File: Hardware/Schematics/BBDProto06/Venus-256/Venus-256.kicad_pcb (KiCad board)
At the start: 2 copper layers, 172.7 x 109.2 mm, 189 parts, among them J1 RaspberryPi header, J10 S08, J11 S09, J12 S10, J13 S11, J14 S12, J15 S13, J16 S14, J17 S15, J18 S16, J2 ARM JTAG, J23 S01, J24 S02, J25 S03, J26 S04, J27 S05, J28 S06, J29 S07, J3 S01, J30 S08, J31 S09, J32 S10, J33 S11, J34 S12, J35 S13, J36 S14, J37 S15, J38 S16, J4 S02, J40 S01, J41 S02, J42 S03, J43 S04, J44 S05, J45 S06, J46 S07, J47 S08, J48 S09, J49 S10, J5 S03, J50 S11, J51 S12, J52 S13, J53 S14, J54 S15, J55 S16, J57 S01, J58 S02, J59 S03, J6 S04, J60 S04, J61 S05, J62 S06, J63 S07, J64 S08, J65 S09, J66 S10, J67 S11, J68 S12, J69 S13, J7 S05, J70 S14, J71 S15, J72 S16, J8 S06, J9 S07, U1 ADG715, U2 AD7616, U3 ATSAME70Q21A-AN, U4 AD7616, U5 AD7616, U6 AD7616, U7 ATSAME70Q21A-AN

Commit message: Added a 5th cell-slave
Added a 5th cell-slave
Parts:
- removed C1, C13, C16, C3, C38, C39, C41, C45, C48, C6, C7, C9: 10uF, Capacitor_SMD:C_0603_1608Metric_Pad0.84x1.00mm_HandSolder
- removed C10, C12, C15, C2, C37, C4, C40, C42, C44, C47, C5, C8: 0.1uF, Capacitor_SMD:C_0603_1608Metric_Pad0.84x1.00mm_HandSolder
- removed C11, C43: 10uF,X5R, Capacitor_SMD:C_0603_1608Metric_Pad0.84x1.00mm_HandSolder
- removed C14, C46: 0.1uF,X8R, Capacitor_SMD:C_0603_1608Metric_Pad0.84x1.00mm_HandSolder
- removed J10, J30, J47, J64: S08, Connector_Wire:SolderWirePad_single_0-8mmDrill
- removed J11, J31, J48, J65: S09, Connector_Wire:SolderWirePad_single_0-8mmDrill
- removed J12, J32, J49, J66: S10, Connector_Wire:SolderWirePad_single_0-8mmDrill
- removed J13, J33, J50, J67: S11, Connector_Wire:SolderWirePad_single_0-8mmDrill
- removed J14, J34, J51, J68: S12, Connector_Wire:SolderWirePad_single_0-8mmDrill
- removed J15, J35, J52, J69: S13, Connector_Wire:SolderWirePad_single_0-8mmDrill
- removed J16, J36, J53, J70: S14, Connector_Wire:SolderWirePad_single_0-8mmDrill
- removed J17, J37, J54, J71: S15, Connector_Wire:SolderWirePad_single_0-8mmDrill
- removed J18, J38, J55, J72: S16, Connector_Wire:SolderWirePad_single_0-8mmDrill
- removed J23, J3, J40, J57: S01, Connector_Wire:SolderWirePad_single_0-8mmDrill
- removed J24, J4, J41, J58: S02, Connector_Wire:SolderWirePad_single_0-8mmDrill
- removed J25, J42, J5, J59: S03, Connector_Wire:SolderWirePad_single_0-8mmDrill
- removed J26, J43, J6, J60: S04, Connector_Wire:SolderWirePad_single_0-8mmDrill
- removed J27, J44, J61, J7: S05, Connector_Wire:SolderWirePad_single_0-8mmDrill
- removed J28, J45, J62, J8: S06, Connector_Wire:SolderWirePad_single_0-8mmDrill
- removed J29, J46, J63, J9: S07, Connector_Wire:SolderWirePad_single_0-8mmDrill
- removed TP5: ADC_REF_OUT, TestPoint:TestPoint_Pad_1.5x1.5mm
- removed U4: AD7616, Package_QFP:LQFP-80_14x14mm_P0.65mm
- added C1001: 10uF, Capacitor_SMD:C_0603_1608Metric_Pad0.84x1.00mm_HandSolder, F.Cu at (-15.2, -43.2)
- added C1002: 0.1uF, Capacitor_SMD:C_0603_1608Metric_Pad0.84x1.00mm_HandSolder, F.Cu at (-15.2, -40.6)
- added C1003: 10uF, Capacitor_SMD:C_0603_1608Metric_Pad0.84x1.00mm_HandSolder, F.Cu at (-15.2, -38.1)
- added C1004: 0.1uF, Capacitor_SMD:C_0603_1608Metric_Pad0.84x1.00mm_HandSolder, F.Cu at (-15.2, -35.6)
- added C1005: 0.1uF, Capacitor_SMD:C_0603_1608Metric_Pad0.84x1.00mm_HandSolder, F.Cu at (15.2, -38.1)
- added C1006: 10uF, Capacitor_SMD:C_0603_1608Metric_Pad0.84x1.00mm_HandSolder, F.Cu at (15.2, -35.6)
- added C1007: 10uF, Capacitor_SMD:C_0603_1608Metric_Pad0.84x1.00mm_HandSolder, F.Cu at (-2.54, -27.9)
- added C1008: 0.1uF, Capacitor_SMD:C_0603_1608Metric_Pad0.84x1.00mm_HandSolder, F.Cu at (-2.54, -25.4)
- added C1009: 10uF, Capacitor_SMD:C_0603_1608Metric_Pad0.84x1.00mm_HandSolder, F.Cu at (-2.54, -55.9)
- added C1010: 0.1uF, Capacitor_SMD:C_0603_1608Metric_Pad0.84x1.00mm_HandSolder, F.Cu at (-2.54, -53.3)
- added C1011: 10uF,X5R, Capacitor_SMD:C_0603_1608Metric_Pad0.84x1.00mm_HandSolder, F.Cu at (2.54, -27.9)
- added C1012: 0.1uF, Capacitor_SMD:C_0603_1608Metric_Pad0.84x1.00mm_HandSolder, F.Cu at (2.54, -55.9)
- added C1013: 10uF, Capacitor_SMD:C_0603_1608Metric_Pad0.84x1.00mm_HandSolder, F.Cu at (2.54, -53.3)
- added C1014: 0.1uF,X8R, Capacitor_SMD:C_0603_1608Metric_Pad0.84x1.00mm_HandSolder, F.Cu at (2.54, -25.4)
- added C1015: 0.1uF, Capacitor_SMD:C_0603_1608Metric_Pad0.84x1.00mm_HandSolder, F.Cu at (15.2, -43.2)
- added C1016: 10uF, Capacitor_SMD:C_0603_1608Metric_Pad0.84x1.00mm_HandSolder, F.Cu at (15.2, -40.6)
- added C401: 10uF, Capacitor_SMD:C_0603_1608Metric_Pad0.84x1.00mm_HandSolder, F.Cu at (31.8, -76.2)
- added C402: 0.1uF, Capacitor_SMD:C_0603_1608Metric_Pad0.84x1.00mm_HandSolder, F.Cu at (31.8, -73.7)
- added C403: 10uF, Capacitor_SMD:C_0603_1608Metric_Pad0.84x1.00mm_HandSolder, F.Cu at (31.8, -69.8)
- added C404: 0.1uF, Capacitor_SMD:C_0603_1608Metric_Pad0.84x1.00mm_HandSolder, F.Cu at (31.8, -67.3)
- added C405: 0.1uF, Capacitor_SMD:C_0603_1608Metric_Pad0.84x1.00mm_HandSolder, F.Cu at (61.0, -71.1)
- added C406: 10uF, Capacitor_SMD:C_0603_1608Metric_Pad0.84x1.00mm_HandSolder, F.Cu at (61.0, -68.6)
- added C407: 10uF, Capacitor_SMD:C_0603_1608Metric_Pad0.84x1.00mm_HandSolder, F.Cu at (43.2, -61.0)
- added C408: 0.1uF, Capacitor_SMD:C_0603_1608Metric_Pad0.84x1.00mm_HandSolder, F.Cu at (43.2, -58.4)
- added C409: 10uF, Capacitor_SMD:C_0603_1608Metric_Pad0.84x1.00mm_HandSolder, F.Cu at (43.2, -88.9)
- added C410: 0.1uF, Capacitor_SMD:C_0603_1608Metric_Pad0.84x1.00mm_HandSolder, F.Cu at (43.2, -86.4)
- added C411: 10uF,X5R, Capacitor_SMD:C_0603_1608Metric_Pad0.84x1.00mm_HandSolder, F.Cu at (48.3, -61.0)
- added C412: 0.1uF, Capacitor_SMD:C_0603_1608Metric_Pad0.84x1.00mm_HandSolder, F.Cu at (48.3, -88.9)
- added C413: 10uF, Capacitor_SMD:C_0603_1608Metric_Pad0.84x1.00mm_HandSolder, F.Cu at (48.3, -86.4)
- added C414: 0.1uF,X8R, Capacitor_SMD:C_0603_1608Metric_Pad0.84x1.00mm_HandSolder, F.Cu at (48.3, -58.4)
- added C415: 0.1uF, Capacitor_SMD:C_0603_1608Metric_Pad0.84x1.00mm_HandSolder, F.Cu at (61.0, -76.2)
- added C416: 10uF, Capacitor_SMD:C_0603_1608Metric_Pad0.84x1.00mm_HandSolder, F.Cu at (61.0, -73.7)
- added C605: 0.1uF, Capacitor_SMD:C_0603_1608Metric_Pad0.84x1.00mm_HandSolder, F.Cu at (111.8, 48.3)
- added C606: 10uF, Capacitor_SMD:C_0603_1608Metric_Pad0.84x1.00mm_HandSolder, F.Cu at (111.8, 50.8)
- added C607: 10uF, Capacitor_SMD:C_0603_1608Metric_Pad0.84x1.00mm_HandSolder, F.Cu at (94.0, 58.4)
- added C608: 0.1uF, Capacitor_SMD:C_0603_1608Metric_Pad0.84x1.00mm_HandSolder, F.Cu at (94.0, 61.0)
- added C609: 10uF, Capacitor_SMD:C_0603_1608Metric_Pad0.84x1.00mm_HandSolder, F.Cu at (94.0, 30.5)
- added C610: 0.1uF, Capacitor_SMD:C_0603_1608Metric_Pad0.84x1.00mm_HandSolder, F.Cu at (94.0, 33.0)
- added C611: 10uF,X5R, Capacitor_SMD:C_0603_1608Metric_Pad0.84x1.00mm_HandSolder, F.Cu at (99.1, 58.4)
- added C612: 0.1uF, Capacitor_SMD:C_0603_1608Metric_Pad0.84x1.00mm_HandSolder, F.Cu at (99.1, 30.5)
- added C613: 10uF, Capacitor_SMD:C_0603_1608Metric_Pad0.84x1.00mm_HandSolder, F.Cu at (99.1, 33.0)
- added C614: 0.1uF,X8R, Capacitor_SMD:C_0603_1608Metric_Pad0.84x1.00mm_HandSolder, F.Cu at (99.1, 61.0)
- added C615: 0.1uF, Capacitor_SMD:C_0603_1608Metric_Pad0.84x1.00mm_HandSolder, F.Cu at (111.8, 43.2)
- added C616: 10uF, Capacitor_SMD:C_0603_1608Metric_Pad0.84x1.00mm_HandSolder, F.Cu at (111.8, 45.7)
- added TP1001: S01, TestPoint:TestPoint_Pad_1.5x1.5mm, B.Cu at (19.1, -59.7)
- added TP1002: S02, TestPoint:TestPoint_Pad_1.5x1.5mm, B.Cu at (6.35, -59.7)
- added TP1003: S03, TestPoint:TestPoint_Pad_1.5x1.5mm, B.Cu at (-6.35, -59.7)
- added TP1004: S04, TestPoint:TestPoint_Pad_1.5x1.5mm, B.Cu at (-19.1, -59.7)
- added TP1005: S05, TestPoint:TestPoint_Pad_1.5x1.5mm, B.Cu at (19.1, -47.0)
- added TP1006: S06, TestPoint:TestPoint_Pad_1.5x1.5mm, B.Cu at (6.35, -47.0)
- added TP1007: S07, TestPoint:TestPoint_Pad_1.5x1.5mm, B.Cu at (-6.35, -47.0)
- added TP1008: S08, TestPoint:TestPoint_Pad_1.5x1.5mm, B.Cu at (-19.1, -47.0)
- added TP1009: S09, TestPoint:TestPoint_Pad_1.5x1.5mm, B.Cu at (19.1, -34.3)
- added TP1010: S10, TestPoint:TestPoint_Pad_1.5x1.5mm, B.Cu at (6.35, -34.3)
- added TP1011: S11, TestPoint:TestPoint_Pad_1.5x1.5mm, B.Cu at (-6.35, -34.3)
- added TP1012: S12, TestPoint:TestPoint_Pad_1.5x1.5mm, B.Cu at (-19.1, -34.3)
- added TP1013: S13, TestPoint:TestPoint_Pad_1.5x1.5mm, B.Cu at (19.1, -21.6)
- added TP1014: S14, TestPoint:TestPoint_Pad_1.5x1.5mm, B.Cu at (6.35, -21.6)
- added TP1015: S15, TestPoint:TestPoint_Pad_1.5x1.5mm, B.Cu at (-6.35, -21.6)
- added TP1016: S16, TestPoint:TestPoint_Pad_1.5x1.5mm, B.Cu at (-19.1, -21.6)
- added TP1017: ADC_REF_OUT, TestPoint:TestPoint_Pad_1.5x1.5mm, F.Cu at (7.62, -25.4)
- added TP401: S01, TestPoint:TestPoint_Pad_1.5x1.5mm, B.Cu at (64.8, -92.7)
- added TP402: S02, TestPoint:TestPoint_Pad_1.5x1.5mm, B.Cu at (52.1, -92.7)
- added TP403: S03, TestPoint:TestPoint_Pad_1.5x1.5mm, B.Cu at (39.4, -92.7)
- added TP404: S04, TestPoint:TestPoint_Pad_1.5x1.5mm, B.Cu at (26.7, -92.7)
- added TP405: S05, TestPoint:TestPoint_Pad_1.5x1.5mm, B.Cu at (64.8, -80.0)
- added TP406: S06, TestPoint:TestPoint_Pad_1.5x1.5mm, B.Cu at (52.1, -80.0)
- added TP407: S07, TestPoint:TestPoint_Pad_1.5x1.5mm, B.Cu at (39.4, -80.0)
- added TP408: S08, TestPoint:TestPoint_Pad_1.5x1.5mm, B.Cu at (26.7, -80.0)
- added TP409: S09, TestPoint:TestPoint_Pad_1.5x1.5mm, B.Cu at (64.8, -67.3)
- added TP410: S10, TestPoint:TestPoint_Pad_1.5x1.5mm, B.Cu at (52.1, -67.3)
- added TP411: S11, TestPoint:TestPoint_Pad_1.5x1.5mm, B.Cu at (39.4, -67.3)
- added TP412: S12, TestPoint:TestPoint_Pad_1.5x1.5mm, B.Cu at (26.7, -67.3)
- added TP413: S13, TestPoint:TestPoint_Pad_1.5x1.5mm, B.Cu at (64.8, -54.6)
- added TP414: S14, TestPoint:TestPoint_Pad_1.5x1.5mm, B.Cu at (52.1, -54.6)
- added TP415: S15, TestPoint:TestPoint_Pad_1.5x1.5mm, B.Cu at (39.4, -54.6)
- added TP416: S16, TestPoint:TestPoint_Pad_1.5x1.5mm, B.Cu at (26.7, -54.6)
- added TP601: S01, TestPoint:TestPoint_Pad_1.5x1.5mm, B.Cu at (102.9, 52.1)
- added TP602: S02, TestPoint:TestPoint_Pad_1.5x1.5mm, B.Cu at (102.9, 26.7)
- added TP603: S03, TestPoint:TestPoint_Pad_1.5x1.5mm, B.Cu at (90.2, 26.7)
- added TP604: S04, TestPoint:TestPoint_Pad_1.5x1.5mm, B.Cu at (77.5, 26.7)
- added TP605: S05, TestPoint:TestPoint_Pad_1.5x1.5mm, B.Cu at (115.6, 39.4)
- added TP606: S06, TestPoint:TestPoint_Pad_1.5x1.5mm, B.Cu at (102.9, 39.4)
- added TP607: S07, TestPoint:TestPoint_Pad_1.5x1.5mm, B.Cu at (90.2, 39.4)
- added TP608: S08, TestPoint:TestPoint_Pad_1.5x1.5mm, B.Cu at (77.5, 39.4)
- added TP609: S09, TestPoint:TestPoint_Pad_1.5x1.5mm, B.Cu at (115.6, 52.1)
- added TP610: S10, TestPoint:TestPoint_Pad_1.5x1.5mm, B.Cu at (115.6, 26.7)
- added TP611: S11, TestPoint:TestPoint_Pad_1.5x1.5mm, B.Cu at (90.2, 52.1)
- added TP612: S12, TestPoint:TestPoint_Pad_1.5x1.5mm, B.Cu at (77.5, 52.1)
- added TP613: S13, TestPoint:TestPoint_Pad_1.5x1.5mm, B.Cu at (115.6, 64.8)
- added TP614: S14, TestPoint:TestPoint_Pad_1.5x1.5mm, B.Cu at (102.9, 64.8)
- added TP615: S15, TestPoint:TestPoint_Pad_1.5x1.5mm, B.Cu at (90.2, 64.8)
- added TP616: S16, TestPoint:TestPoint_Pad_1.5x1.5mm, B.Cu at (77.5, 64.8)
- added TP617: ADC_REF_OUT, TestPoint:TestPoint_Pad_1.5x1.5mm, F.Cu at (104.1, 61.0)
- added TP701: S01, TestPoint:TestPoint_Pad_1.5x1.5mm, B.Cu at (120.6, 244.4)
- added TP702: S02, TestPoint:TestPoint_Pad_1.5x1.5mm, B.Cu at (124.9, 250.0)
- added TP703: S03, TestPoint:TestPoint_Pad_1.5x1.5mm, B.Cu at (120.6, 238.9)
- added TP704: S04, TestPoint:TestPoint_Pad_1.5x1.5mm, B.Cu at (129.2, 250.0)
- added TP705: S05, TestPoint:TestPoint_Pad_1.5x1.5mm, B.Cu at (124.9, 244.4)
- added TP706: S06, TestPoint:TestPoint_Pad_1.5x1.5mm, B.Cu at (129.2, 244.4)
- added TP707: S07, TestPoint:TestPoint_Pad_1.5x1.5mm, B.Cu at (124.9, 238.9)
- added TP708: S08, TestPoint:TestPoint_Pad_1.5x1.5mm, B.Cu at (133.6, 250.0)
- added TP709: S09, TestPoint:TestPoint_Pad_1.5x1.5mm, B.Cu at (129.2, 238.9)
- added TP710: S10, TestPoint:TestPoint_Pad_1.5x1.5mm, B.Cu at (137.9, 250.0)
- added TP711: S11, TestPoint:TestPoint_Pad_1.5x1.5mm, B.Cu at (133.6, 244.4)
- added TP712: S12, TestPoint:TestPoint_Pad_1.5x1.5mm, B.Cu at (137.9, 244.4)
- added TP713: S13, TestPoint:TestPoint_Pad_1.5x1.5mm, B.Cu at (133.6, 238.9)
- added TP714: S14, TestPoint:TestPoint_Pad_1.5x1.5mm, B.Cu at (142.2, 250.0)
- added TP715: S15, TestPoint:TestPoint_Pad_1.5x1.5mm, B.Cu at (137.9, 238.9)
- added TP716: S16, TestPoint:TestPoint_Pad_1.5x1.5mm, B.Cu at (120.6, 250.0)
- added TP801: S01, TestPoint:TestPoint_Pad_1.5x1.5mm, B.Cu at (-92.4, 136.4)
- added TP802: S02, TestPoint:TestPoint_Pad_1.5x1.5mm, B.Cu at (-92.4, 130.9)
- added TP803: S03, TestPoint:TestPoint_Pad_1.5x1.5mm, B.Cu at (-88.1, 136.4)
- added TP804: S04, TestPoint:TestPoint_Pad_1.5x1.5mm, B.Cu at (-92.4, 125.3)
- added TP805: S05, TestPoint:TestPoint_Pad_1.5x1.5mm, B.Cu at (-83.8, 136.4)
- added TP806: S06, TestPoint:TestPoint_Pad_1.5x1.5mm, B.Cu at (-88.1, 130.9)
- added TP807: S07, TestPoint:TestPoint_Pad_1.5x1.5mm, B.Cu at (-83.8, 130.9)
- added TP808: S08, TestPoint:TestPoint_Pad_1.5x1.5mm, B.Cu at (-88.1, 125.3)
- added TP809: S09, TestPoint:TestPoint_Pad_1.5x1.5mm, B.Cu at (-79.5, 136.4)
- added TP810: S10, TestPoint:TestPoint_Pad_1.5x1.5mm, B.Cu at (-83.8, 125.3)
- added TP811: S11, TestPoint:TestPoint_Pad_1.5x1.5mm, B.Cu at (-75.2, 136.4)
- added TP812: S12, TestPoint:TestPoint_Pad_1.5x1.5mm, B.Cu at (-79.5, 130.9)
- added TP813: S13, TestPoint:TestPoint_Pad_1.5x1.5mm, B.Cu at (-75.2, 130.9)
- added TP814: S14, TestPoint:TestPoint_Pad_1.5x1.5mm, B.Cu at (-79.5, 125.3)
- added TP815: S15, TestPoint:TestPoint_Pad_1.5x1.5mm, B.Cu at (-70.8, 136.4)
- added TP816: S16, TestPoint:TestPoint_Pad_1.5x1.5mm, B.Cu at (-75.2, 125.3)
- added U1001: AD7616, Package_QFP:LQFP-80_14x14mm_P0.65mm, F.Cu at (0.00, -40.3)
- added U601: AD7616, Package_QFP:LQFP-80_14x14mm_P0.65mm, F.Cu at (96.5, 45.7)
- moved C714 307.3 mm to (190.4, 291.0)
- moved C703 303.4 mm to (214.9, 291.0)
- moved C716 298.2 mm to (202.4, 301.9)
- moved C702 296.1 mm to (206.9, 301.9)
- moved C711 295.6 mm to (190.1, 296.4)
- moved C701 292.3 mm to (210.1, 296.4)
- moved C715 290.9 mm to (210.3, 291.0)
- moved C710 289.8 mm to (197.8, 301.9)
- moved C708 288.9 mm to (205.5, 291.0)
- moved C704 287.5 mm to (188.7, 301.9)
- moved C712 285.0 mm to (205.5, 296.4)
- moved C709 284.2 mm to (200.9, 296.4)
- moved C706 280.3 mm to (200.9, 291.0)
- moved C713 280.3 mm to (196.6, 291.0)
- moved C707 276.2 mm to (193.2, 301.9)
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- renumbered C17 to C501, C18 to C502, C19 to C503, C20 to C504, C21 to C505, C22 to C506, C23 to C507, C24 to C508, C25 to C509, C26 to C510, C27 to C511, C28 to C512, C29 to C513, C30 to C514, C31 to C515, C32 to C516, C33 to C601, C34 to C602, C35 to C603, C36 to C604, C49 to C701, C50 to C702, C51 to C703, C52 to C704, C53 to C705, C54 to C706, C55 to C707, C56 to C708, C57 to C709, C58 to C710, C59 to C711, C60 to C712, C61 to C713, C62 to C714, C63 to C715, C64 to C716, C65 to C801, C66 to C802, C67 to C803, C68 to C804, C69 to C805, C70 to C806, C71 to C807, C72 to C808, C73 to C809, C74 to C810, C75 to C811, C76 to C812, C77 to C813, C78 to C814, C79 to C815, C80 to C816, C81 to C901, C82 to C902, C83 to C903, C84 to C904, C85 to C905, C86 to C906, C87 to C907, C88 to C908, C89 to C909, C90 to C910, C91 to C911, C92 to C912, C93 to C913, C94 to C914, C95 to C915, C96 to C916, D1 to D501, D2 to D901, L1 to L501, L2 to L901, R5 to R501, R6 to R901, TP1 to TP417, TP4 to TP501, TP3 to TP502, TP2 to TP503, TP6 to TP717, TP7 to TP817, TP10 to TP901, TP9 to TP902, TP8 to TP903, U2 to U401, U3 to U501, U5 to U701, U6 to U801, U7 to U901
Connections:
- U901 pad 12: (no net) -> /CellSlave-02A/SDI
- U901 pad 13: (no net) -> /CellSlave-02A/SDOA
- U901 pad 130: (no net) -> /CellSlave-02A/SCLK
- U901 pad 133: (no net) -> /CellMaster-02/SPI1_NPCS0
- U901 pad 4: (no net) -> /CellMaster-02/ADC_CONVST0
- U901 pad 46: (no net) -> /CellMaster-02/ADC_BUSY0
- U901 pad 70: (no net) -> /CellMaster-02/ADC_RESET
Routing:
- net Net-(P07-04A1-Pad1): track 110.2 -> 107.0 mm
- net Net-(P07-02A1-Pad1): track 2.24 -> 0.00 mm
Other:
- board text added: "Bio Balance Detector #6 Rev. A (2018-05-02) | Andras Fuchs (andras.fuchs@gmail.com)"
- board text removed: "Bio Balance Detector #6 Rev. C (2018-04-27) | Flat Panel Detector | Andras Fuchs (andras.fuchs@gmail.com)"

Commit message: Updated the AD7616 and its Cell Slave schematics
Updated the AD7616 and its Cell Slave schematics
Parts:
- removed the C711 at (190.1, 296.4)
- added C712: 10uF,X5R, Capacitor_SMD:C_0603_1608Metric_Pad0.84x1.00mm_HandSolder, F.Cu at (99.1, 109.2)
- C405, C415: value 0.1uF -> 10uF
- C406, C413: value 10uF -> 0.1uF
- C411: value 10uF,X5R -> 0.1uF,X8R
- C412: value 0.1uF -> 10uF,X5R
- C414: value 0.1uF,X8R -> 0.1uF
- J201: renamed from J1; footprint Connector_PinHeader_2.54mm:PinHeader_2x20_P2.54mm_Vertical -> Connector_PinHeader_2.54mm:PinHeader_2x20_P2.54mm_Horizontal
- J301: renamed from J2; footprint Connector_PinHeader_2.54mm:PinHeader_2x10_P2.54mm_Vertical -> Connector_PinHeader_2.54mm:PinHeader_2x10_P2.54mm_Horizontal
- moved TP801 265.4 mm to (166.4, 77.5)
- moved TP805 254.4 mm to (166.4, 90.2)
- moved TP802 251.8 mm to (153.7, 77.5)
- moved TP809 248.1 mm to (166.4, 102.9)
- moved TP806 245.2 mm to (153.7, 90.2)
- moved TP813 242.0 mm to (166.4, 115.6)
- moved C708 241.5 mm to (94.0, 83.8)
- moved C702 240.7 mm to (81.3, 96.5)
- moved C707 240.2 mm to (94.0, 81.3)
- moved C713 240.0 mm to (99.1, 81.3)
- moved C701 239.9 mm to (81.3, 94.0)
- moved TP810 238.5 mm to (153.7, 102.9)
- moved C814 238.2 mm to (162.6, 94.0)
- moved TP803 236.5 mm to (141.0, 77.5)
- moved TP814 233.3 mm to (153.7, 115.6)
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- renumbered C1007 to C1005, C1008 to C1006, C1009 to C1007, C1010 to C1008, C1006 to C1009, C1005 to C1010, C1014 to C1011, C1011 to C1012, C1012 to C1013, C1015 to C1014, C1013 to C1015, C607 to C605, C608 to C606, C609 to C607, C610 to C608, C606 to C609, C605 to C610, C614 to C611, C611 to C612, C612 to C613, C615 to C614, C613 to C615, C707 to C705, C708 to C706, C709 to C707, C710 to C708, C706 to C709, C705 to C710, C714 to C711, C712 to C713, C715 to C714, C713 to C715, C807 to C805, C808 to C806, C809 to C807, C810 to C808, C806 to C809, C805 to C810, C814 to C811, C811 to C812, C812 to C813, C815 to C814, C813 to C815, R1 to R301, R2 to R302, R3 to R303, R4 to R304, U1 to U101
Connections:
- C1002 pad 1: GND -> /RaspberryPiGPIOHeader/DC_POWER_5V0
- C1002 pad 2: /RaspberryPiGPIOHeader/DC_POWER_5V0 -> GND
- C1013 pad 1: GND -> Net-(C1013-Pad1)
- C1013 pad 2: Net-(C1012-Pad2) -> GND
- C1014 pad 1: GND -> Net-(C1014-Pad1)
- C1014 pad 2: Net-(C1015-Pad2) -> GND
- C1015 pad 1: GND -> Net-(C1013-Pad1)
- C1015 pad 2: Net-(C1012-Pad2) -> GND
- C1016 pad 1: GND -> Net-(C1014-Pad1)
- C1016 pad 2: Net-(C1015-Pad2) -> GND
- C402 pad 1: GND -> /RaspberryPiGPIOHeader/DC_POWER_5V0
- C402 pad 2: /RaspberryPiGPIOHeader/DC_POWER_5V0 -> GND
- C405 pad 2: /RaspberryPiGPIOHeader/DC_POWER_3V3 -> /RaspberryPiGPIOHeader/DC_POWER_5V0
- C406 pad 2: /RaspberryPiGPIOHeader/DC_POWER_3V3 -> /RaspberryPiGPIOHeader/DC_POWER_5V0
- C409 pad 2: /RaspberryPiGPIOHeader/DC_POWER_5V0 -> /RaspberryPiGPIOHeader/DC_POWER_3V3
- C410 pad 2: /RaspberryPiGPIOHeader/DC_POWER_5V0 -> /RaspberryPiGPIOHeader/DC_POWER_3V3
- C412 pad 1: GND -> Net-(C412-Pad1)
- C412 pad 2: Net-(C412-Pad2) -> GND
- C413 pad 1: GND -> Net-(C413-Pad1)
- C413 pad 2: Net-(C412-Pad2) -> GND
- C415 pad 1: GND -> Net-(C413-Pad1)
- C415 pad 2: Net-(C415-Pad2) -> GND
- C416 pad 1: GND -> Net-(C414-Pad1)
- C416 pad 2: Net-(C415-Pad2) -> GND
- C602 pad 1: GND -> /RaspberryPiGPIOHeader/DC_POWER_5V0
- C602 pad 2: /RaspberryPiGPIOHeader/DC_POWER_5V0 -> GND
- C613 pad 1: GND -> Net-(C613-Pad1)
- C613 pad 2: Net-(C612-Pad2) -> GND
- C614 pad 1: GND -> Net-(C614-Pad1)
- C614 pad 2: Net-(C615-Pad2) -> GND
- C615 pad 1: GND -> Net-(C613-Pad1)
- C615 pad 2: Net-(C612-Pad2) -> GND
- C616 pad 1: GND -> Net-(C614-Pad1)
- C616 pad 2: Net-(C615-Pad2) -> GND
- C702 pad 1: GND -> /RaspberryPiGPIOHeader/DC_POWER_5V0
- C702 pad 2: /RaspberryPiGPIOHeader/DC_POWER_5V0 -> GND
- C713 pad 1: GND -> Net-(C713-Pad1)
- C713 pad 2: Net-(C712-Pad2) -> GND
- C714 pad 1: GND -> Net-(C714-Pad1)
- C714 pad 2: Net-(C715-Pad2) -> GND
- C715 pad 1: GND -> Net-(C713-Pad1)
- C715 pad 2: Net-(C712-Pad2) -> GND
- C716 pad 1: GND -> Net-(C714-Pad1)
- C716 pad 2: Net-(C715-Pad2) -> GND
- C802 pad 1: GND -> /RaspberryPiGPIOHeader/DC_POWER_5V0
- C802 pad 2: /RaspberryPiGPIOHeader/DC_POWER_5V0 -> GND
- C813 pad 1: GND -> Net-(C813-Pad1)
- C813 pad 2: Net-(C812-Pad2) -> GND
- C814 pad 1: GND -> Net-(C814-Pad1)
- C814 pad 2: Net-(C815-Pad2) -> GND
- C815 pad 1: GND -> Net-(C813-Pad1)
- C815 pad 2: Net-(C812-Pad2) -> GND
- C816 pad 1: GND -> Net-(C814-Pad1)
- C816 pad 2: Net-(C815-Pad2) -> GND
- TP417 pad 1: Net-(C414-Pad1) -> Net-(C411-Pad1)
- U1001 pad 52: Net-(C1015-Pad2) -> Net-(C1014-Pad1)
- U1001 pad 70: Net-(C1012-Pad2) -> Net-(C1013-Pad1)
- U401 pad 31: Net-(C411-Pad1) -> Net-(C412-Pad1)
- U401 pad 33: Net-(C414-Pad1) -> Net-(C411-Pad1)
- U401 pad 52: Net-(C415-Pad2) -> Net-(C414-Pad1)
- U401 pad 70: Net-(C412-Pad2) -> Net-(C413-Pad1)
- U601 pad 52: Net-(C615-Pad2) -> Net-(C614-Pad1)
- U601 pad 70: Net-(C612-Pad2) -> Net-(C613-Pad1)
- U701 pad 52: Net-(C715-Pad2) -> Net-(C714-Pad1)
- U701 pad 70: Net-(C712-Pad2) -> Net-(C713-Pad1)
- U801 pad 52: Net-(C815-Pad2) -> Net-(C814-Pad1)
- U801 pad 70: Net-(C812-Pad2) -> Net-(C813-Pad1)
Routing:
- net (no net): track 1674.9 -> 0.00 mm
- net Net-(TP609-Pad1): track 0.00 -> 482.1 mm
- net Net-(TP614-Pad1): track 0.00 -> 482.1 mm
- net Net-(TP401-Pad1): track 0.00 -> 300.7 mm
- net Net-(TP403-Pad1): track 0.00 -> 300.7 mm
- net Net-(TP404-Pad1): track 0.00 -> 300.2 mm
- net Net-(TP402-Pad1): track 0.00 -> 300.2 mm
- net Net-(TP408-Pad1): track 0.00 -> 292.6 mm
- net Net-(TP406-Pad1): track 0.00 -> 292.6 mm
- net Net-(TP407-Pad1): track 0.00 -> 125.1 mm
- net Net-(TP405-Pad1): track 0.00 -> 125.1 mm

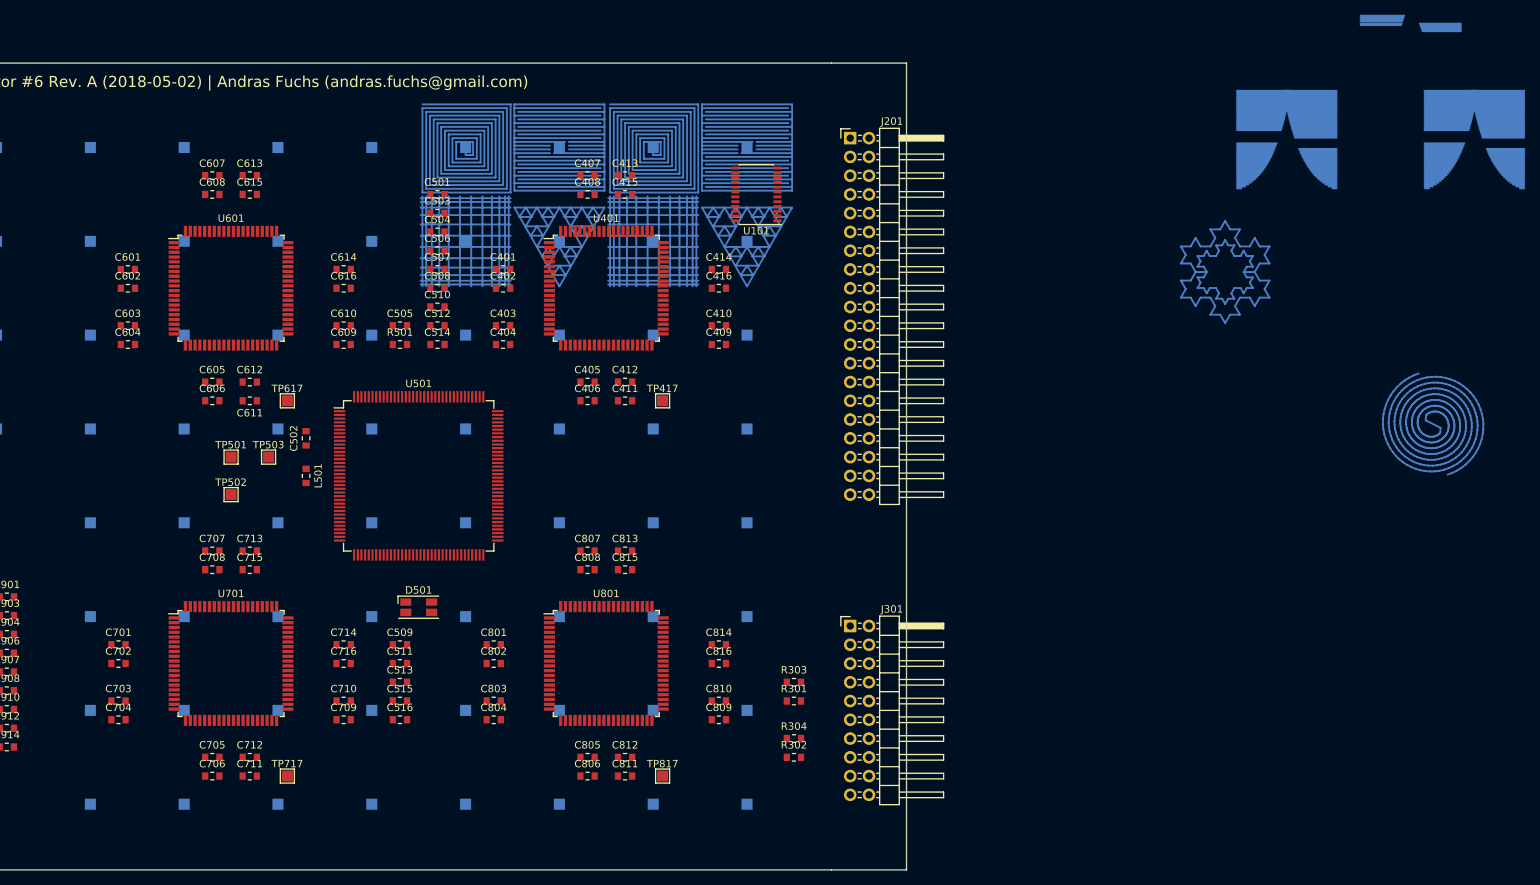
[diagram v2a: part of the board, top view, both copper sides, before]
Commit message: Added the half of the fractal antennas
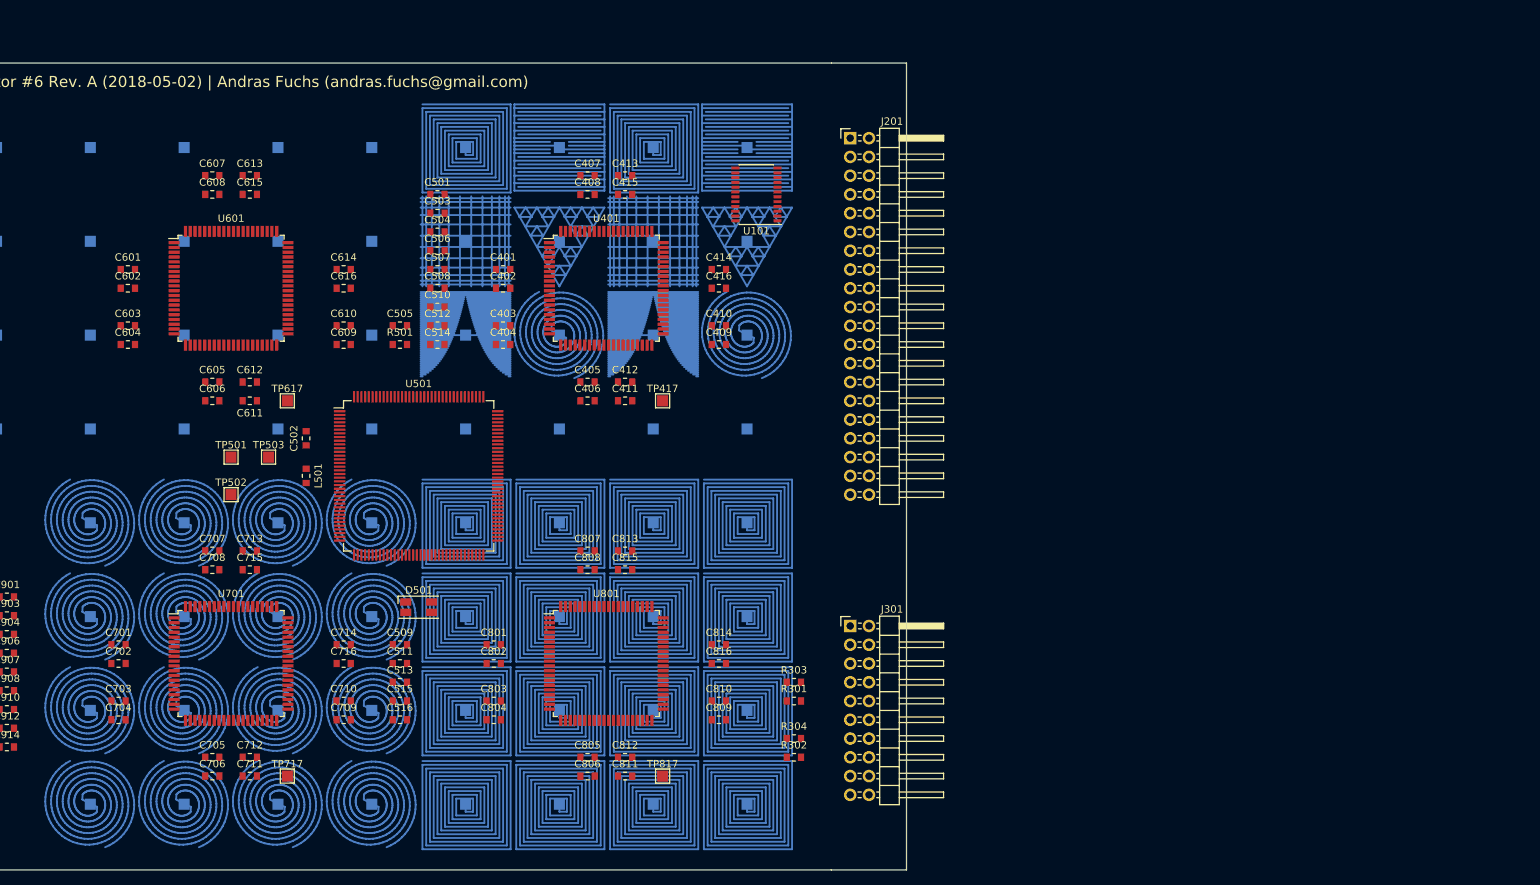
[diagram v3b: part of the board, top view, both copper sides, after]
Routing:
- net Net-(TP609-Pad1): track 482.1 -> 0.00 mm
- net Net-(TP614-Pad1): track 482.1 -> 0.00 mm
- net Net-(TP412-Pad1): track 0.00 -> 384.1 mm
- net Net-(TP410-Pad1): track 0.00 -> 384.1 mm
- net Net-(TP811-Pad1): track 0.00 -> 300.2 mm
- net Net-(TP808-Pad1): track 0.00 -> 300.2 mm
- net Net-(TP804-Pad1): track 0.00 -> 300.2 mm
- net Net-(TP803-Pad1): track 0.00 -> 300.2 mm
- net Net-(TP816-Pad1): track 0.00 -> 300.2 mm
- net Net-(TP815-Pad1): track 0.00 -> 300.2 mm
- net Net-(TP802-Pad1): track 0.00 -> 300.2 mm
- net Net-(TP814-Pad1): track 0.00 -> 300.2 mm
- net Net-(TP807-Pad1): track 0.00 -> 300.2 mm
- net Net-(TP806-Pad1): track 0.00 -> 300.2 mm
- net Net-(TP810-Pad1): track 0.00 -> 300.2 mm
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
